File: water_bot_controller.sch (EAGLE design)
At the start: 55 parts

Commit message: added microcontroller module, cleaned up relay driver module
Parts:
- removed LED2, LED3, LED4: (no value), led:LED
- removed R10, R11, R12: 10k, rcl:R-US_R0603
- removed R7, R8, R9: 0 ohm, rcl:R-US_R0603
- added C1: 1uF, rcl:C-USC0603
- added C2, C6: 0.1uF, rcl:C-USC0603
- added C3, C5: 4.7uF, rcl:C-USC1206
- added C4: 10uF, rcl:C-USC1206
- added D1: MMBD4148DICT, LEDdynamics:MMBD4148DICT
- added R22, R23: 10K, rcl:R-US_R0603
- added R24: 10 ohm, rcl:R-US_R0603
- added U$1: PSOC_4000, stovelite:PSOC_4000
- added U2: LM3480IM3-5.0, LEDdynamics:LM3480IM3-5.0
- IC1: value (none) -> ULN2803A
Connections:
- removed net 6C: IC1.O6
- removed net 7C: IC1.O7
- removed net 8C: IC1.O8
- removed net N$10: IC1.I7, R8.2
- removed net N$11: IC1.I8, R9.2
- removed net N$12: IC1.I2, R3.2
- removed net N$18: LED4.A, R12.1
- removed net N$19: LED3.A, R11.1
- removed net N$20: LED2.A, R10.1
- removed net N$9 (its old number): IC1.I6, R7.2
- removed net P6: R12.2, R7.1
- removed net P7: R11.2, R8.1
- removed net P8: R10.2, R9.1
- new net N$37: C1.2, U$1.VCCD
- new net N$38: D1.C, R24.1
- new net N$39: C4.1, R24.2, U2.IN
- new net N$6: R3.2
- new net P0.2: R22.1, R23.2, U$1.P0.2
- new net SCLK: U$1.P3.1
- new net SDAT: U$1.P3.0
- new net VDD: C2.1, C3.1, C5.1, C6.1, R22.2, U$1.VDD, U2.OUT
- net +12V: now also D1.A
- net GND: now also C1.1, C2.2, C3.2, C4.2, C5.2, C6.2, LED13.C, R23.1, U$1.VSS, U2.GND; no longer LED2.C, LED3.C, LED4.C
- net N$35: now also R21.2
- net P1: now also U$1.P2.0
- net P2: now also U$1.P1.7
- net P3: now also U$1.P1.6
- net P4: now also U$1.P1.3
- net P5: now also U$1.P1.2
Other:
- note added: "Dedicated Microcontroller, PSOC-4000 SOIC-16"
- note added: "Input Voltage Conditioning 3.3V"
- note added: "Input Voltage Monitor"
- note added: "LM3480IM3-5.0"
- note added: "Linear Voltage Regulator 3.3V, 100mA"
- note added: "Microcontroller Module"
- note added: "Relay Driver Module"
- note removed: "UProc Output to Relay Input"
- moved on the sheet: F1, F2, F3, F4, F5, LED1, LED10, LED11, LED12, LED13, LED5, LED6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

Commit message: cleaned up relay module
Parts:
- removed LED11, LED12, LED13: (no value), led:LED
- removed R18, R19, R20, R21: 10K, rcl:R-US_R0603
- added LED2, LED3, LED4: (no value), led:LED
- added R10, R7, R8, R9: 10K, rcl:R-US_R0603
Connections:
- net N$3 renamed R1
- removed net N$1 (its old number): RELAY_1.5, TP1.TP
- removed net N$21: RELAY_2.5, TP3.TP
- removed net N$23: F2.2, R18.2, TP4.TP
- removed net N$24: LED10.A, R18.1
- removed net N$25: RELAY_3.5, TP5.TP
- removed net N$27: F3.2, R19.2, TP6.TP
- removed net N$28: LED11.A, R19.1
- removed net N$29: RELAY_4.5, TP7.TP
- removed net N$31: F4.2, R20.2, TP8.TP
- removed net N$32: LED12.A, R20.1
- removed net N$33: RELAY_5.5, TP9.TP
- removed net N$35: F5.2, R21.2, TP10.TP
- removed net N$36: LED13.A, R21.1
- new net N$11: LED3.A, R8.1
- new net N$18: LED4.A, R9.1
- new net N$20: LED10.A, R10.1
- new net N$4: LED2.A, R7.1
- new net R2: F2.2, R7.2, TP4.TP
- new net R3: F3.2, R8.2, TP6.TP
- new net R4: F4.2, R9.2, TP8.TP
- new net R5: F5.2, R10.2, TP10.TP
- net 1C: now also RELAY_1.5, TP1.TP
- net 2C: now also RELAY_2.5, TP3.TP
- net 3C: now also RELAY_3.5, TP5.TP
- net 4C: now also RELAY_4.5, TP7.TP
- net 5C: now also RELAY_5.5, TP9.TP
- net GND: now also LED2.C, LED3.C, LED4.C; no longer LED11.C, LED12.C, LED13.C
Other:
- note added: "Dedicated Microcontroller Module"
- note added: "Relay Module"
- note removed: "Microcontroller Module"
- note removed: "Relays"
- moved on the sheet: F1, F2, F3, F4, F5, LED1, LED10, R1, RELAY_1, RELAY_2, RELAY_3, RELAY_4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

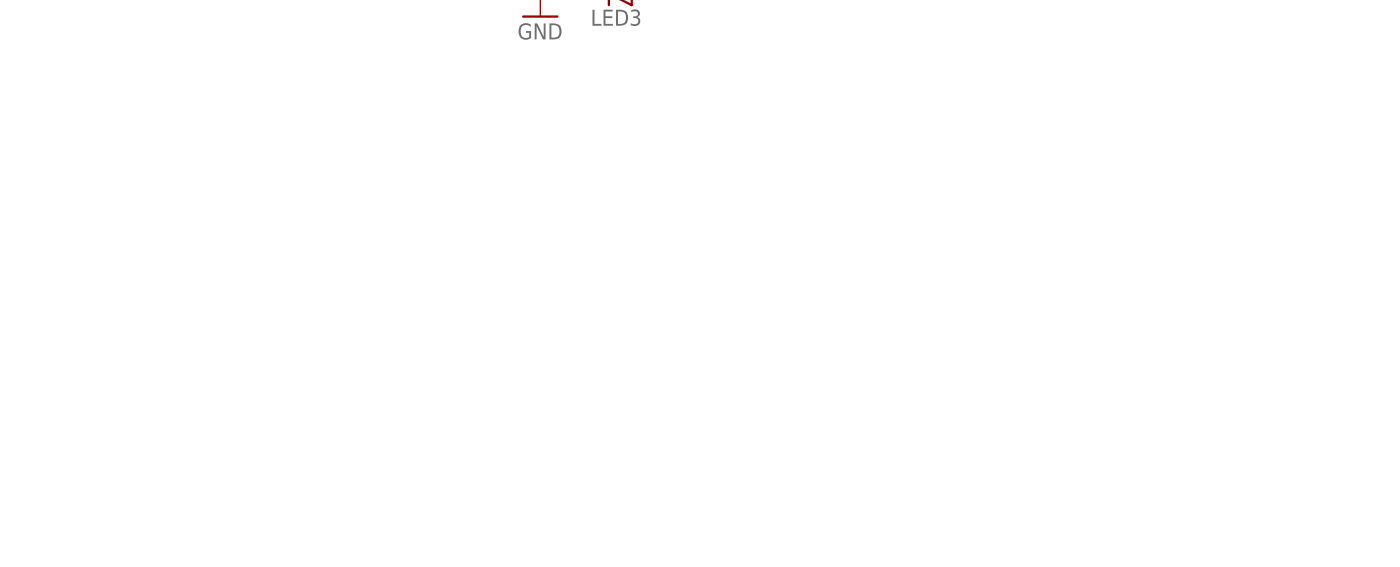
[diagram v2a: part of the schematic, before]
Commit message: spec'd pwr/sig conns, added pushbuttons to schematic
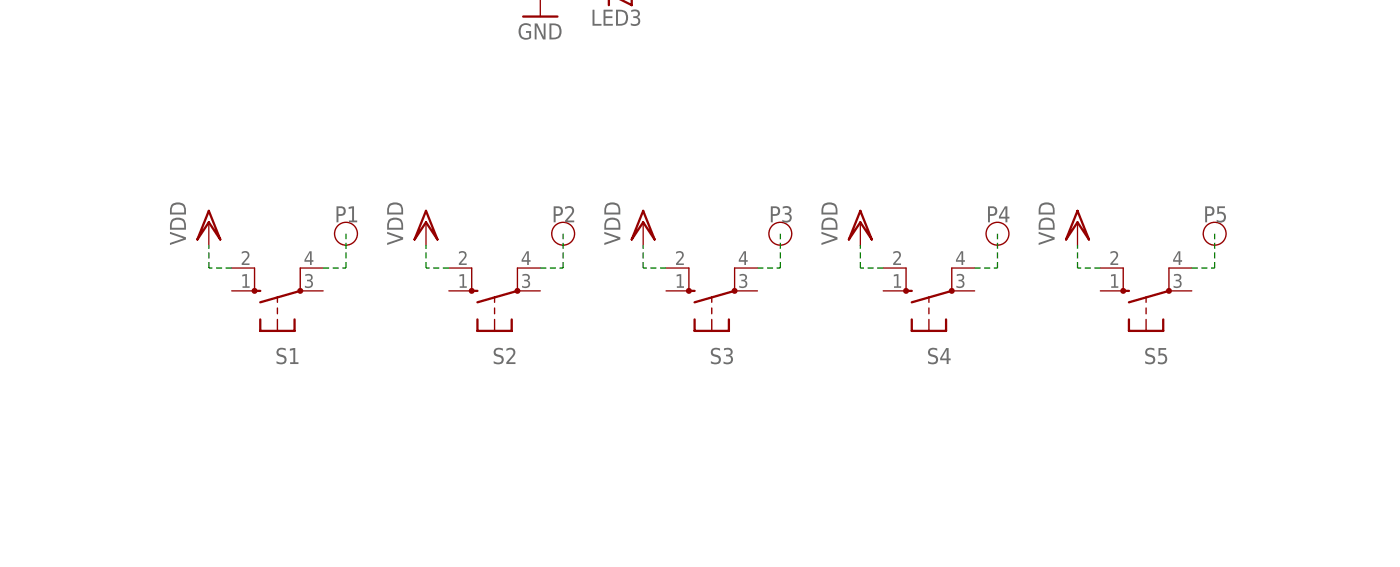
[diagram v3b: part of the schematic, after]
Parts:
- added S1, S2, S3, S4, S5: (no value), switch-omron:10-XX
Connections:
- net P1: now also S1.P1
- net P2: now also S2.P1
- net P3: now also S3.P1
- net P4: now also S4.P1
- net P5: now also S5.P1
- net VDD: now also S1.S1, S2.S1, S3.S1, S4.S1, S5.S1
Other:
- note added: "Pushbutton Switches"
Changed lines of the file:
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@@
 <part name="LED10" library="led" library_urn="urn:adsk.eagle:library:259" deviceset="LED" device="" package3d_urn="urn:adsk.eagle:package:15825/1"/>
 <part name="GND7" library="supply1" library_urn="urn:adsk.eagle:library:371" deviceset="GND" device=""/>
+<part name="S1" library="switch-omron" library_urn="urn:adsk.eagle:library:377" deviceset="10-XX" device="" package3d_urn="urn:adsk.eagle:package:27496/1"/>
+<part name="VDD4" library="supply1" library_urn="urn:adsk.eagle:library:371" deviceset="VDD" device=""/>
+<part name="S2" library="switch-omron" library_urn="urn:adsk.eagle:library:377" deviceset="10-XX" device="" package3d_urn="urn:adsk.eagle:package:27496/1"/>
+<part name="VDD5" library="supply1" library_urn="urn:adsk.eagle:library:371" deviceset="VDD" device=""/>
+<part name="S3" library="switch-omron" library_urn="urn:adsk.eagle:library:377" deviceset="10-XX" device="" package3d_urn="urn:adsk.eagle:package:27496/1"/>
+<part name="VDD6" library="supply1" library_urn="urn:adsk.eagle:library:371" deviceset="VDD" device=""/>
+<part name="S4" library="switch-omron" library_urn="urn:adsk.eagle:library:377" deviceset="10-XX" device="" package3d_urn="urn:adsk.eagle:package:27496/1"/>
+<part name="VDD7" library="supply1" library_urn="urn:adsk.eagle:library:371" deviceset="VDD" device=""/>
+<part name="S5" library="switch-omron" library_urn="urn:adsk.eagle:library:377" deviceset="10-XX" device="" package3d_urn="urn:adsk.eagle:package:27496/1"/>
+<part name="VDD8" library="supply1" library_urn="urn:adsk.eagle:library:371" deviceset="VDD" device=""/>
 </parts>
 <sheets>
@@
 <wire x1="138.43" y1="175.26" x2="138.43" y2="12.7" width="0.1524" layer="90" style="longdash"/>
 <text x="194.31" y="167.64" size="2.54" layer="90">Relay Module</text>
+<circle x="166.37" y="-6.35" radius="1.27" width="0.1524" layer="94"/>
+<circle x="190.5" y="-6.35" radius="1.27" width="0.1524" layer="94"/>
+<circle x="214.63" y="-6.35" radius="1.27" width="0.1524" layer="94"/>
+<circle x="238.76" y="-6.35" radius="1.27" width="0.1524" layer="94"/>
+<circle x="262.89" y="-6.35" radius="1.27" width="0.1524" layer="94"/>
+<wire x1="143.51" y1="7.62" x2="267.97" y2="7.62" width="0.1524" layer="90" style="longdash"/>
+<wire x1="267.97" y1="7.62" x2="267.97" y2="-22.86" width="0.1524" layer="90" style="longdash"/>
+<wire x1="267.97" y1="-22.86" x2="143.51" y2="-22.86" width="0.1524" layer="90" style="longdash"/>
+<wire x1="143.51" y1="-22.86" x2="143.51" y2="7.62" width="0.1524" layer="90" style="longdash"/>
+<text x="198.12" y="2.54" size="2.54" layer="90">Pushbutton Switches</text>
 </plain>
 <instances>
@@
 <instance part="LED10" gate="G$1" x="265.43" y="69.85" rot="R270"/>
 <instance part="GND7" gate="1" x="255.27" y="67.31"/>
+<instance part="S1" gate="1" x="158.75" y="-12.7" rot="R90"/>
+<instance part="VDD4" gate="G$1" x="151.13" y="-5.08"/>
+<instance part="S2" gate="1" x="182.88" y="-12.7" rot="R90"/>
+<instance part="VDD5" gate="G$1" x="175.26" y="-5.08"/>
+<instance part="S3" gate="1" x="207.01" y="-12.7" rot="R90"/>
+<instance part="VDD6" gate="G$1" x="199.39" y="-5.08"/>
+<instance part="S4" gate="1" x="231.14" y="-12.7" rot="R90"/>
+<instance part="VDD7" gate="G$1" x="223.52" y="-5.08"/>
+<instance part="S5" gate="1" x="255.27" y="-12.7" rot="R90"/>
+<instance part="VDD8" gate="G$1" x="247.65" y="-5.08"/>
 </instances>
 <busses>
@@
 <label x="60.96" y="128.27" size="1.27" layer="95"/>
 </segment>
+<segment>
+<pinref part="S5" gate="1" pin="P1"/>
+<wire x1="260.35" y1="-10.16" x2="262.89" y2="-10.16" width="0.1524" layer="91" style="longdash"/>
+<wire x1="262.89" y1="-10.16" x2="262.89" y2="-6.35" width="0.1524" layer="91" style="longdash"/>
+<label x="261.62" y="-5.08" size="1.778" layer="95"/>
+</segment>
 </net>
 <net name="P4" class="0">
@@
 <label x="60.96" y="137.16" size="1.27" layer="95"/>
 </segment>
+<segment>
+<pinref part="S4" gate="1" pin="P1"/>
+<wire x1="236.22" y1="-10.16" x2="238.76" y2="-10.16" width="0.1524" layer="91" style="longdash"/>
+<wire x1="238.76" y1="-10.16" x2="238.76" y2="-6.35" width="0.1524" layer="91" style="longdash"/>
+<label x="237.49" y="-5.08" size="1.778" layer="95"/>
+</segment>
 </net>
 <net name="P3" class="0">
@@
 <label x="60.96" y="146.05" size="1.27" layer="95"/>
 </segment>
+<segment>
+<pinref part="S3" gate="1" pin="P1"/>
+<wire x1="212.09" y1="-10.16" x2="214.63" y2="-10.16" width="0.1524" layer="91" style="longdash"/>
+<wire x1="214.63" y1="-10.16" x2="214.63" y2="-6.35" width="0.1524" layer="91" style="longdash"/>
+<label x="213.36" y="-5.08" size="1.778" layer="95"/>
+</segment>
 </net>
 <net name="P2" class="0">
@@
 <label x="60.96" y="154.94" size="1.27" layer="95"/>
 </segment>
+<segment>
+<pinref part="S2" gate="1" pin="P1"/>
+<wire x1="187.96" y1="-10.16" x2="190.5" y2="-10.16" width="0.1524" layer="91" style="longdash"/>
+<wire x1="190.5" y1="-10.16" x2="190.5" y2="-6.35" width="0.1524" layer="91" style="longdash"/>
+<label x="189.23" y="-5.08" size="1.778" layer="95"/>
+</segment>
 </net>
 <net name="P1" class="0">
@@
 <wire x1="66.04" y1="162.56" x2="58.42" y2="162.56" width="0.1524" layer="91" style="longdash"/>
 <label x="60.96" y="163.83" size="1.27" layer="95"/>
+</segment>
+<segment>
+<pinref part="S1" gate="1" pin="P1"/>
+<wire x1="163.83" y1="-10.16" x2="166.37" y2="-10.16" width="0.1524" layer="91" style="longdash"/>
+<wire x1="166.37" y1="-10.16" x2="166.37" y2="-6.35" width="0.1524" layer="91" style="longdash"/>
+<label x="165.1" y="-5.08" size="1.778" layer="95"/>
 </segment>
 </net>
@@
 <junction x="119.38" y="87.63"/>
 </segment>
-</net>
+<segment>
+<pinref part="S1" gate="1" pin="S1"/>
+<pinref part="VDD4" gate="G$1" pin="VDD"/>
+<wire x1="153.67" y1="-10.16" x2="151.13" y2="-10.16" width="0.1524" layer="91" style="longdash"/>
+<wire x1="151.13" y1="-10.16" x2="151.13" y2="-7.62" width="0.1524" layer="91" style="longdash"/>
+</segment>
+<segment>
+<pinref part="S2" gate="1" pin="S1"/>
+<pinref part="VDD5" gate="G$1" pin="VDD"/>
+<wire x1="177.8" y1="-10.16" x2="175.26" y2="-10.16" width="0.1524" layer="91" style="longdash"/>
+<wire x1="175.26" y1="-10.16" x2="175.26" y2="-7.62" width="0.1524" layer="91" style="longdash"/>
+</segment>
+<segment>
+<pinref part="S3" gate="1" pin="S1"/>
+<pinref part="VDD6" gate="G$1" pin="VDD"/>
+<wire x1="201.93" y1="-10.16" x2="199.39" y2="-10.16" width="0.1524" layer="91" style="longdash"/>
+<wire x1="199.39" y1="-10.16" x2="199.39" y2="-7.62" width="0.1524" layer="91" style="longdash"/>
+</segment>
+<segment>
+<pinref part="S4" gate="1" pin="S1"/>
+<pinref part="VDD7" gate="G$1" pin="VDD"/>
+<wire x1="226.06" y1="-10.16" x2="223.52" y2="-10.16" width="0.1524" layer="91" style="longdash"/>
+<wire x1="223.52" y1="-10.16" x2="223.52" y2="-7.62" width="0.1524" layer="91" style="longdash"/>
+</segment>
+<segment>
+<pinref part="S5" gate="1" pin="S1"/>
+<pinref part="VDD8" gate="G$1" pin="VDD"/>
+<wire x1="250.19" y1="-10.16" x2="247.65" y2="-10.16" width="0.1524" layer="91" style="longdash"/>
+<wire x1="247.65" y1="-10.16" x2="247.65" y2="-7.62" width="0.1524" layer="91" style="longdash"/>
+</segment>
+</net>

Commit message: added optional particle photon headers
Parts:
- added R18, R19, R20, R21, R25, R26, R27, R28: 0 ohm, rcl:R-US_R0603
- added U$2: PHOTON_WITH_HEADERS, Spark:PHOTON_WITH_HEADERS
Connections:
- removed net SCLK: U$1.P3.1
- removed net SDAT: U$1.P3.0
- new net N$21: R26.1, U$2.D2
- new net N$22: R27.1, U$2.D1
- new net N$23: R18.1, U$2.3V3
- new net N$24: R19.1, U$2.D6
- new net N$25: R20.1, U$2.D5
- new net N$26: R21.1, U$2.D4
- new net N$27: R25.1, U$2.D3
- new net N$28: R28.1, U$2.D0
- new net SCL: R27.2, U$1.P3.1
- new net SDA: R28.2, U$1.P3.0
- net GND: now also U$2.GND@2, U$2.GND@21
- net P1: now also R19.2
- net P2: now also R20.2
- net P3: now also R21.2
- net P4: now also R25.2
- net P5: now also R26.2
- net VDD: now also R18.2
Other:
- note added: "Optional Microcontroller Module"
- moved on the sheet: F1, F2, F3, F4, F5, LED1, LED10, LED2, LED3, LED4, R1, R10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

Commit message: added i2c isolation circuitry, replaced leds, and added test points
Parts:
- removed D1: MMBD4148DICT, LEDdynamics:MMBD4148DICT
- removed R22, R23: 10K, rcl:R-US_R0603
- added +12V, GND, I2C_3V3, I2C_GND, I2C_SCL, I2C_SDA, RELAY1, RELAY2, RELAY3, RELAY4, RELAY5, RELAY_GND: WIREPAD3,17/1,3, wirepad:WIREPAD3,17/1,3
- added C10: 4.7uF, rcl:C-USC1206
- added C7, C8: 10uF, rcl:C-USC1206
- added C9: 0.1uF, rcl:C-USC0603
- added R11, R12, R29, R30: 1K, rcl:R-US_R0603
- added TP11, TP12, TP13, TP14, TP15, TP16, TP17, TP18, TP19, TP20, TP21, TP22, TP23: PTR1B2,54, testpad:PTR1B2,54
- added U$3: ISO1540, ISO1540:ISO1540
- LED1, LED10, LED2, LED3, LED4, LED5, LED6, LED7, LED8: device led:LED -> led:LEDCHIP-LED0603
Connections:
- removed net GND: C1.1, C2.2, C3.2, C4.2, C5.2, C6.2, IC1.GND, LED1.C, LED10.C, LED2.C, LED3.C, LED4.C, LED5.C, LED6.C, LED7.C, LED8.C, LED9.C, R23.1, U$1.VSS, U$2.GND@2, U$2.GND@21, U2.GND
- removed net N$37: C1.2, U$1.VCCD
- removed net N$38: D1.C, R24.1
- removed net P0.2: R22.1, R23.2, U$1.P0.2
- removed net VDD: C2.1, C3.1, C5.1, C6.1, R18.2, R22.2, S1.S1, S2.S1, S3.S1, S4.S1, S5.S1, U$1.VDD, U2.OUT
- new net +3V3: C2.1, C3.1, C5.1, C6.1, C8.1, R18.2, R29.2, R30.2, S1.S1, S2.S1, S3.S1, S4.S1, S5.S1, TP11.TP, U$1.VDD, U$3.VCC2, U2.OUT
- new net 12V_IN: +12V.P, TP21.TP
- new net GND1: C7.2, GND.P, I2C_GND.P, IC1.GND, LED1.C, LED10.C, LED2.C, LED3.C, LED4.C, LED5.C, LED6.C, LED7.C, LED8.C, LED9.C, RELAY_GND.P, TP17.TP, TP18.TP, TP20.TP, U$3.GND1
- new net GND2: C1.2, C10.2, C2.2, C3.2, C4.2, C5.2, C6.2, C8.2, C9.2, U$1.VSS, U$2.GND@2, U$2.GND@21, U$3.GND2, U2.GND
- new net I2C_3V3: C7.1, I2C_3V3.P, R11.2, R12.2, TP23.TP, U$3.VCC1
- new net I2C_SCL: I2C_SCL.P, R12.1, TP19.TP, U$3.SCL1
- new net I2C_SDA: I2C_SDA.P, R11.1, TP22.TP, U$3.SDA1
- new net N$29: C1.1, U$1.VCCD
- net +12V: now also R24.1; no longer D1.A
- net N$14: now also LED5.A; no longer LED8.A
- net N$15: now also LED6.A; no longer LED7.A
- net N$16: now also LED7.A; no longer LED6.A
- net N$17: now also LED8.A; no longer LED5.A
- net N$23: now also C10.1, C9.1
- net R1: now also RELAY1.P, TP12.TP
- net R2: now also RELAY2.P, TP13.TP
- net R3: now also RELAY3.P, TP14.TP
- net R4: now also RELAY4.P, TP15.TP
- net R5: now also RELAY5.P, TP16.TP
- net SCL: now also R30.1, U$3.SCL2
- net SDA: now also R29.1, U$3.SDA2
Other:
- note added: "3V3 Regulator Module"
- note added: "I2C Isolation Module"
- note added: "Physical Connections Module"
- note added: "Pushbutton Switches Module"
- note removed: "Dedicated Microcontroller, PSOC-4000 SOIC-16"
- note removed: "Input Voltage Conditioning 3.3V"
- note removed: "Input Voltage Monitor"
- note removed: "Linear Voltage Regulator 3.3V, 100mA"
- note removed: "Pushbutton Switches"
- moved on the sheet: C1, C2, C3, C4, C5, C6, LED5, LED6, LED7, LED8, R18, R19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
